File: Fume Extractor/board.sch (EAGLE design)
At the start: 17 parts, among them IC2 DW01, IC3 TP4056, T1 FS8205A

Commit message: update
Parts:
- added C3: 22uF, rcl:C-EUC0805
- added C7: 4.7uF, rcl:C-EUC0805
- added D1: SS34, diode:DIODE-DO214AC
- added L1: 22uH, SparkFun-Coils:INDUCTOR-0805-3.3UH
- C2: value 4.7uF -> 22uF
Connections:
- new net 12V: C3.1, C7.1, D1.C
- new net N$10: D1.A, L1.2, U$2.SW
- net 5V: now also L1.1
- net GND: now also C3.2, C7.2
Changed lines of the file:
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@@
 <setting verticaltext="up"/>
 </settings>
-<grid distance="0.05" unitdist="inch" unit="inch" style="lines" multiple="1" display="no" altdistance="0.01" altunitdist="inch" altunit="inch"/>
+<grid distance="50" unitdist="mil" unit="mil" style="lines" multiple="1" display="no" altdistance="0.01" altunitdist="inch" altunit="inch"/>
 <layers>
 <layer number="1" name="Top" color="4" fill="1" visible="no" active="no"/>
@@
 <part name="C6" library="rcl" library_urn="urn:adsk.eagle:library:334" deviceset="C-EU" device="C0805" package3d_urn="urn:adsk.eagle:package:23617/2" value="0.1uF"/>
 <part name="U$2" library="buckboost" deviceset="MT3608" device=""/>
-<part name="C2" library="rcl" library_urn="urn:adsk.eagle:library:334" deviceset="C-EU" device="C0805" package3d_urn="urn:adsk.eagle:package:23617/2" value="4.7uF"/>
+<part name="C2" library="rcl" library_urn="urn:adsk.eagle:library:334" deviceset="C-EU" device="C0805" package3d_urn="urn:adsk.eagle:package:23617/2" value="22uF"/>
 <part name="SUPPLY2" library="SparkFun-PowerSymbols" library_urn="urn:adsk.eagle:library:530" deviceset="5V" device=""/>
 <part name="GND2" library="SparkFun-PowerSymbols" library_urn="urn:adsk.eagle:library:530" deviceset="GND" device=""/>
+<part name="L1" library="SparkFun-Coils" library_urn="urn:adsk.eagle:library:512" deviceset="INDUCTOR" device="-0805-3.3UH" package3d_urn="urn:adsk.eagle:package:37579/1" value="22uH"/>
+<part name="D1" library="diode" deviceset="DIODE-" device="DO214AC" value="SS34"/>
+<part name="C3" library="rcl" library_urn="urn:adsk.eagle:library:334" deviceset="C-EU" device="C0805" package3d_urn="urn:adsk.eagle:package:23617/2" value="22uF"/>
+<part name="GND3" library="SparkFun-PowerSymbols" library_urn="urn:adsk.eagle:library:530" deviceset="GND" device=""/>
+<part name="SUPPLY4" library="SparkFun-PowerSymbols" library_urn="urn:adsk.eagle:library:530" deviceset="12V" device=""/>
+<part name="C7" library="rcl" library_urn="urn:adsk.eagle:library:334" deviceset="C-EU" device="C0805" package3d_urn="urn:adsk.eagle:package:23617/2" value="4.7uF"/>
 </parts>
 <sheets>
 <sheet>
 <plain>
+<text x="185.42" y="20.32" size="2.54" layer="94" font="vector">&gt;CNAME</text>
+<text x="237.49" y="5.08" size="2.54" layer="94" font="vector">&gt;CREVISION</text>
 </plain>
 <instances>
@@
 <instance part="GND2" gate="1" x="148.59" y="66.04" smashed="yes">
 <attribute name="VALUE" x="148.59" y="65.786" size="1.778" layer="96" align="top-center"/>
+</instance>
+<instance part="L1" gate="G$1" x="168.91" y="90.17" smashed="yes" rot="R90">
+<attribute name="NAME" x="166.37" y="91.44" size="1.778" layer="95" font="vector"/>
+<attribute name="VALUE" x="166.37" y="88.9" size="1.778" layer="96" font="vector" align="top-left"/>
+</instance>
+<instance part="D1" gate="G$1" x="187.96" y="90.17" smashed="yes">
+<attribute name="NAME" x="190.5" y="90.6526" size="1.778" layer="95"/>
+<attribute name="VALUE" x="190.5" y="87.8586" size="1.778" layer="96"/>
+</instance>
+<instance part="C3" gate="G$1" x="210.82" y="83.82" smashed="yes">
+<attribute name="NAME" x="212.344" y="84.201" size="1.778" layer="95"/>
+<attribute name="VALUE" x="212.344" y="79.121" size="1.778" layer="96"/>
+</instance>
+<instance part="GND3" gate="1" x="210.82" y="69.85" smashed="yes">
+<attribute name="VALUE" x="210.82" y="69.596" size="1.778" layer="96" align="top-center"/>
+</instance>
+<instance part="SUPPLY4" gate="G$1" x="210.82" y="95.25" smashed="yes">
+<attribute name="VALUE" x="210.82" y="98.044" size="1.778" layer="96" align="bottom-center"/>
+</instance>
+<instance part="C7" gate="G$1" x="201.93" y="83.82" smashed="yes">
+<attribute name="NAME" x="203.454" y="84.201" size="1.778" layer="95"/>
+<attribute name="VALUE" x="203.454" y="79.121" size="1.778" layer="96"/>
 </instance>
 </instances>
@@
 <wire x1="157.48" y1="77.47" x2="160.02" y2="77.47" width="0.1524" layer="91"/>
 </segment>
+<segment>
+<pinref part="C3" gate="G$1" pin="2"/>
+<pinref part="GND3" gate="1" pin="GND"/>
+<wire x1="210.82" y1="78.74" x2="210.82" y2="74.93" width="0.1524" layer="91"/>
+<pinref part="C7" gate="G$1" pin="2"/>
+<wire x1="210.82" y1="74.93" x2="210.82" y2="72.39" width="0.1524" layer="91"/>
+<wire x1="201.93" y1="78.74" x2="201.93" y2="74.93" width="0.1524" layer="91"/>
+<wire x1="201.93" y1="74.93" x2="210.82" y2="74.93" width="0.1524" layer="91"/>
+<junction x="210.82" y="74.93"/>
+</segment>
 </net>
 <net name="5V" class="1">
@@
 <wire x1="157.48" y1="82.55" x2="160.02" y2="82.55" width="0.1524" layer="91"/>
 <pinref part="SUPPLY2" gate="G$1" pin="5V"/>
-<wire x1="157.48" y1="82.55" x2="148.59" y2="82.55" width="0.1524" layer="91"/>
+<wire x1="157.48" y1="82.55" x2="156.21" y2="82.55" width="0.1524" layer="91"/>
+<wire x1="156.21" y1="82.55" x2="148.59" y2="82.55" width="0.1524" layer="91"/>
 <wire x1="148.59" y1="82.55" x2="148.59" y2="90.17" width="0.1524" layer="91"/>
 <junction x="157.48" y="82.55"/>
@@
 <wire x1="148.59" y1="81.28" x2="148.59" y2="82.55" width="0.1524" layer="91"/>
 <junction x="148.59" y="82.55"/>
+<pinref part="L1" gate="G$1" pin="1"/>
+<wire x1="156.21" y1="82.55" x2="156.21" y2="90.17" width="0.1524" layer="91"/>
+<wire x1="156.21" y1="90.17" x2="163.83" y2="90.17" width="0.1524" layer="91"/>
+<junction x="156.21" y="82.55"/>
 </segment>
 </net>
@@
 </segment>
 </net>
+<net name="N$10" class="1">
+<segment>
+<pinref part="L1" gate="G$1" pin="2"/>
+<wire x1="173.99" y1="90.17" x2="181.61" y2="90.17" width="0.1524" layer="91"/>
+<wire x1="181.61" y1="90.17" x2="181.61" y2="82.55" width="0.1524" layer="91"/>
+<pinref part="U$2" gate="G$1" pin="SW"/>
+<wire x1="181.61" y1="82.55" x2="180.34" y2="82.55" width="0.1524" layer="91"/>
+<pinref part="D1" gate="G$1" pin="A"/>
+<wire x1="185.42" y1="90.17" x2="181.61" y2="90.17" width="0.1524" layer="91"/>
+<junction x="181.61" y="90.17"/>
+</segment>
+</net>
+<net name="12V" class="1">
+<segment>
+<pinref part="D1" gate="G$1" pin="C"/>
+<wire x1="190.5" y1="90.17" x2="201.93" y2="90.17" width="0.1524" layer="91"/>
+<pinref part="SUPPLY4" gate="G$1" pin="12V"/>
+<wire x1="201.93" y1="90.17" x2="210.82" y2="90.17" width="0.1524" layer="91"/>
+<wire x1="210.82" y1="90.17" x2="210.82" y2="95.25" width="0.1524" layer="91"/>
+<pinref part="C3" gate="G$1" pin="1"/>
+<wire x1="210.82" y1="86.36" x2="210.82" y2="90.17" width="0.1524" layer="91"/>
+<junction x="210.82" y="90.17"/>
+<pinref part="C7" gate="G$1" pin="1"/>
+<wire x1="201.93" y1="86.36" x2="201.93" y2="90.17" width="0.1524" layer="91"/>
+<junction x="201.93" y="90.17"/>
+</segment>
+</net>

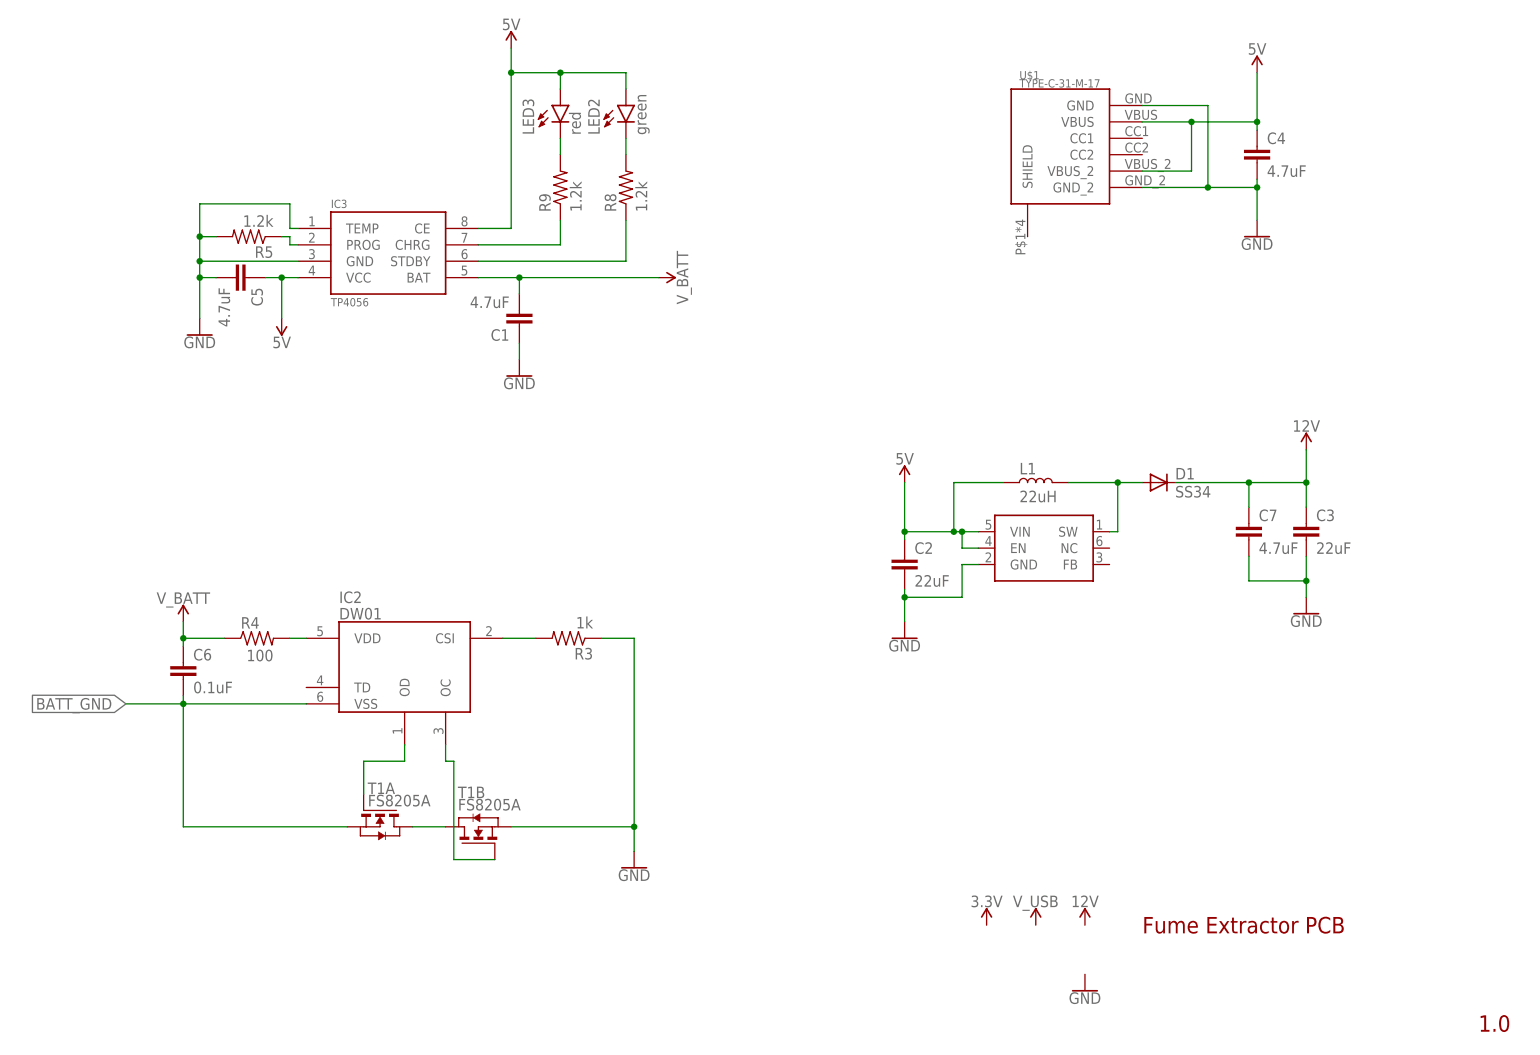
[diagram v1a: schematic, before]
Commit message: MT3608 boost converter circuit complete..?
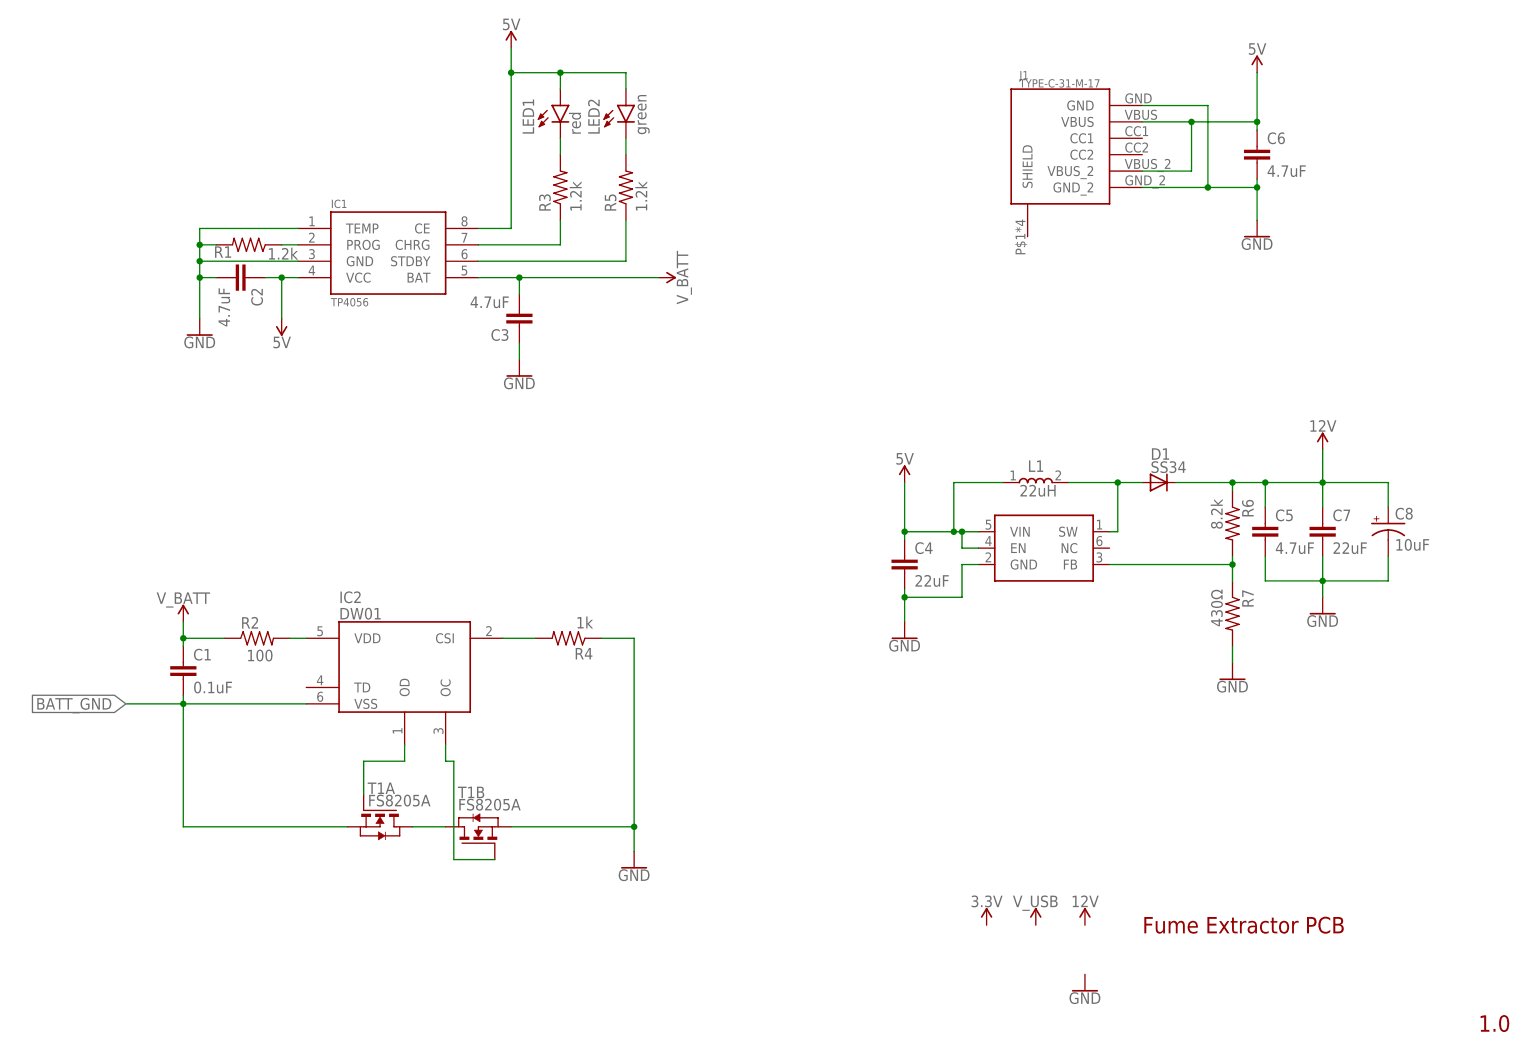
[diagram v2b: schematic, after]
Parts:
- removed R8, R9: 1.2k, rcl:R-US_R0805
- added C8: 10uF, rcl:CPOL-USSMCA
- added R1: 1.2k, rcl:R-US_R0805
- added R2: 100, rcl:R-US_R0805
- added R6: 8.2k, rcl:R-US_R0805
- added R7: 430Ω, rcl:R-US_R0805
- C1: value 4.7uF -> 0.1uF
- C2, C3: value 22uF -> 4.7uF
- C4, C7: value 4.7uF -> 22uF
- C6: value 0.1uF -> 4.7uF
- L1: device SparkFun-Coils:INDUCTOR-0805-3.3UH -> BCIHP0730-220M:BCIHP0730-220M
- R3: value 1k -> 1.2k
- R4: value 100 -> 1k
- renumbered IC3 to IC1, LED3 to LED1, U$1 to J1, U$2 to U1
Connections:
- new net N$12: R6.2, R7.1, U1.FB
- net 12V: now also C5.1, C8.+, R6.1; no longer C3.1
- net 5V: now also C6.1; no longer C5.1
- net BATT_GND: now also C1.2; no longer C6.2
- net GND: now also C3.1, C6.2, C8.-, R1.2, R4.1, R7.2; no longer C1.1, C3.2, R3.1, R5.2
- net N$1: now also R2.2; no longer R4.2
- net N$11: now also R3.2; no longer R9.2
- net N$2: now also R3.1; no longer R9.1
- net N$3: now also R5.1; no longer R8.1
- net N$4: now also R4.2; no longer R3.2
- net N$8: now also R1.1; no longer R5.1
- net N$9: now also R5.2; no longer R8.2
- net V_BATT: now also C1.1, C3.2, R2.1; no longer C1.2, C6.1, R4.1
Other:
- moved on the sheet: C1, C2, C3, C4, C5, C6, C7, R3, R4, R5
